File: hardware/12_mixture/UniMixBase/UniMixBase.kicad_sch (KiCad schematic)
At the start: 145 parts, among them IC1 VNN3NV04PTR-E, IC11 VNN3NV04PTR-E, IC2 VNN3NV04PTR-E, IC3 VNN3NV04PTR-E, IC4 VNN3NV04PTR-E, IC5 VNN3NV04PTR-E, IC6 VNN3NV04PTR-E, IC7 VNN3NV04PTR-E, IC8 VNN3NV04PTR-E, J1 Conn_01x04_Male, J10 Conn_01x03_Pin, J11 Conn_01x02_Male, J12 Conn_01x02_Male, J13 Conn_01x02_Male, J14 Conn_01x04_Male, J18 Conn_01x04_Male, J2 Conn_01x04_Male, J20 Conn_01x04_Male, J21 Conn_01x04_Male, J22 Conn_01x03_Pin, J24 Conn_01x04_Male, J3 Conn_01x04_Male, J31 Conn_01x02_Male, J32 Conn_01x02_Male, J33 Conn_01x02_Male, J4 Conn_01x04_Male, J5 Conn_01x04_Male, J6 Conn_01x03_Pin, J7 Conn_01x04_Male, J8 Conn_01x04_Male, J9 Conn_01x04_Male, U1 NUCLEO-H755, U10 74AHC04, U11 MP1584 DC/DC, U12 TCA9802, U13 TMC2209_SILENTSTEPSTICK, U2 TMC2209_SILENTSTEPSTICK, U3 TMC2209_SILENTSTEPSTICK, U4 TMC2209_SILENTSTEPSTICK, U5 74AHC04, U6 TMC2209_SILENTSTEPSTICK, U7 TMC2209_SILENTSTEPSTICK, U8 MP1584 DC/DC, U9 74AHC04

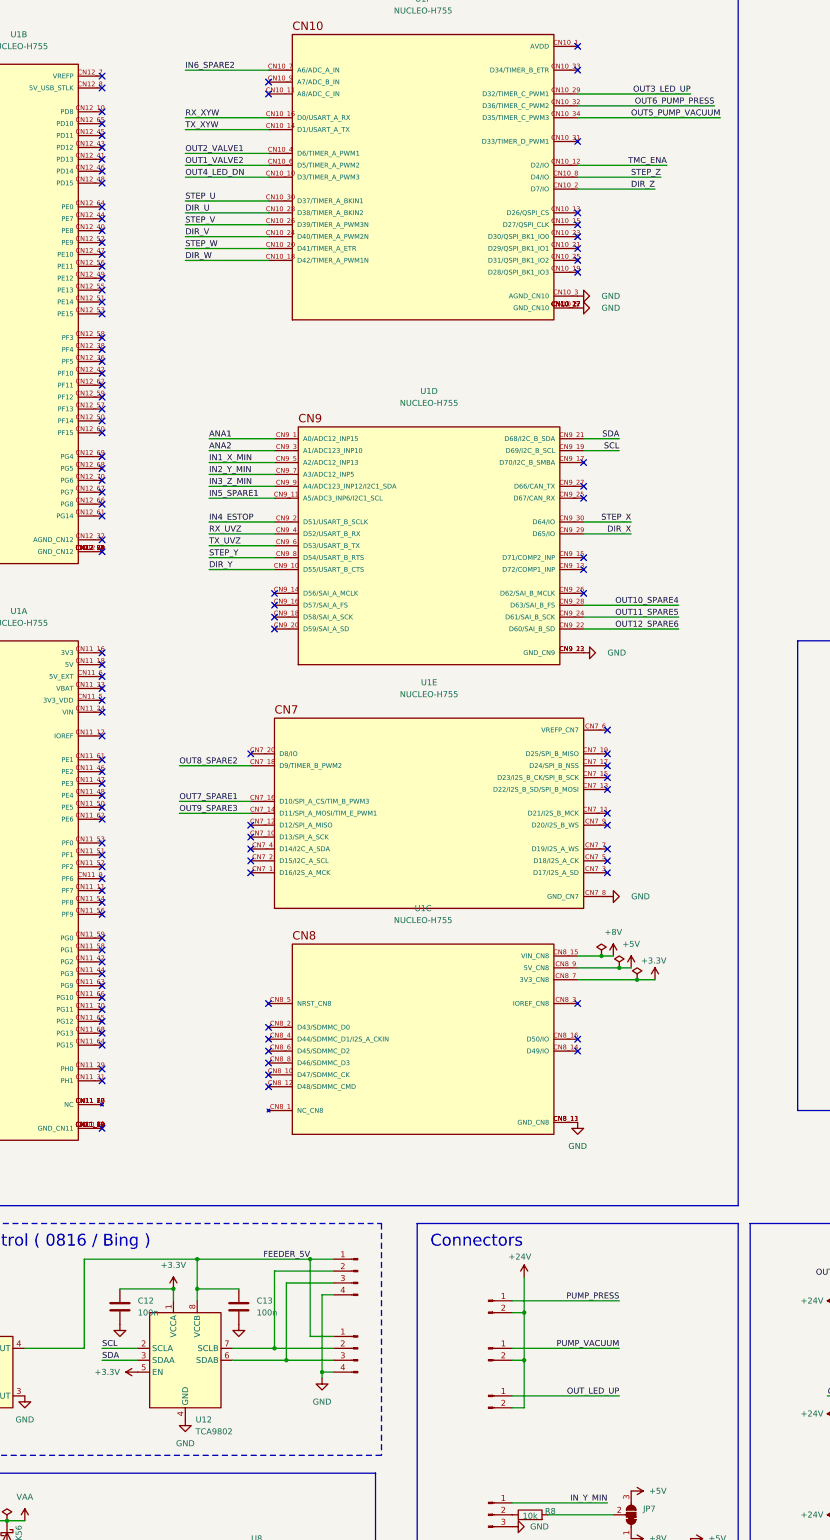
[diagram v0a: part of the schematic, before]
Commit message: Upadtes for Nucleo version
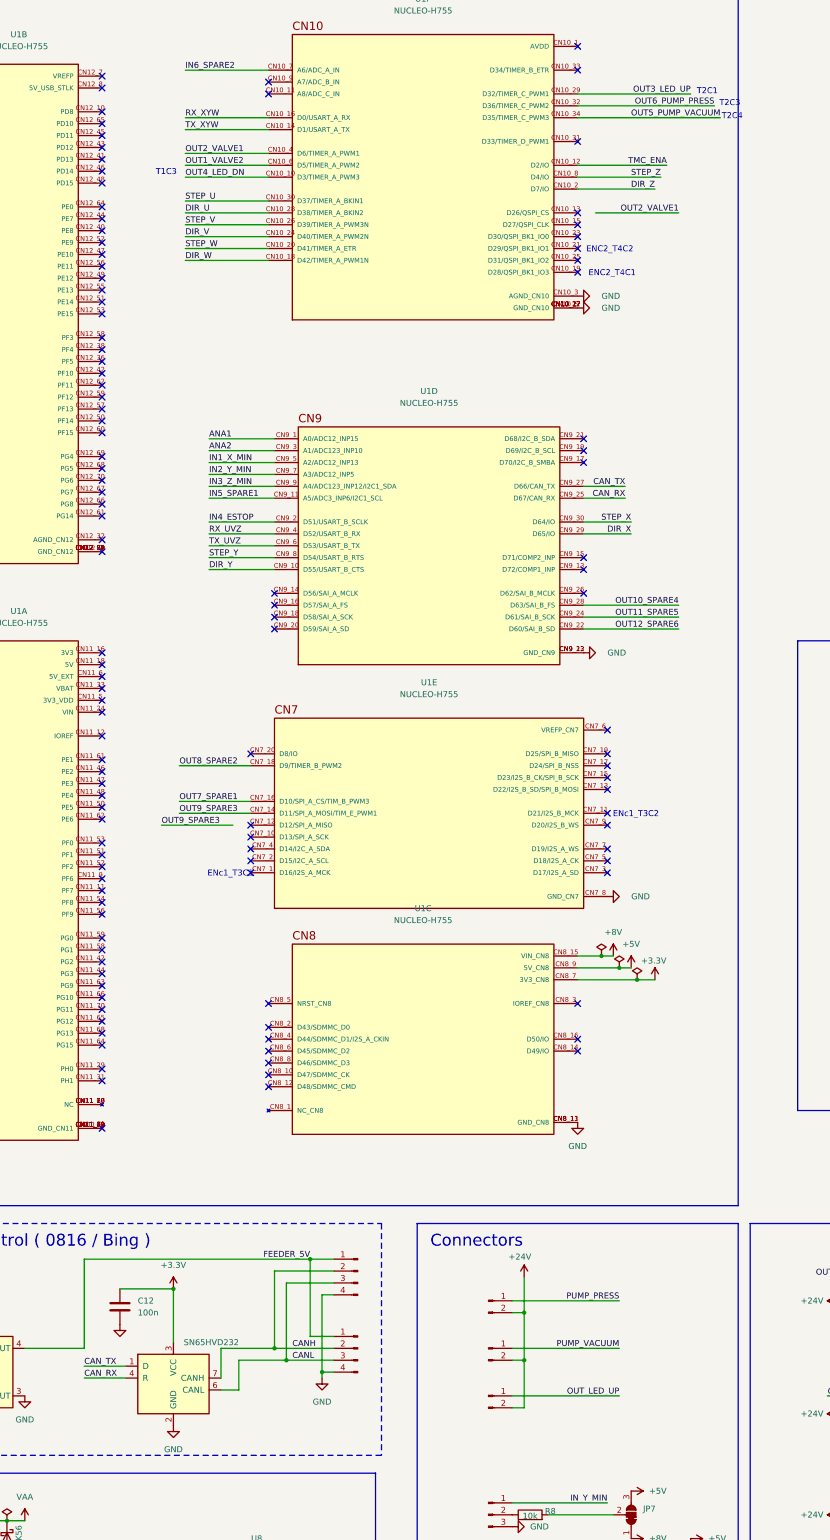
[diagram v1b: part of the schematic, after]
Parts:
- removed C13: 100n, Capacitor_SMD:C_0603_1608Metric, symbol Device:C
- removed U12: TCA9802, Package_SO:VSSOP-8_3x3mm_P0.65mm, symbol Interface:TCA9802
- added U12: SN65HVD232, Package_SO:SOIC-8_3.9x4.9mm_P1.27mm, symbol Interface_CAN_LIN:SN65HVD232
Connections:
- net +3.3V: now also U12.3 (VCC)
- net GND: now also U12.2 (GND)
- net CANL: now reaches J5.3 (Pin_3), J8.3 (Pin_3)
- net CANL: now also U12.6 (CANL)
- net CANH: now reaches J5.2 (Pin_2), J8.2 (Pin_2)
- net CANH: now also U12.7 (CANH)
- net CAN_RX: now reaches U1.CN9_25 (D67/CAN_RX)
- net CAN_RX: now also U12.4 (R)
- net CAN_TX: now reaches U1.CN9_27 (D66/CAN_TX)
- net CAN_TX: now also U12.1 (D)
- net SCL: no longer names the net of U1.CN9_19 (D69/I2C_B_SCL)
- net SDA: no longer names the net of U1.CN9_21 (D68/I2C_B_SDA)
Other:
- note added: "ENC2_T4C1"
- note added: "ENC2_T4C2"
- note added: "ENc1_T3C1"
- note added: "ENc1_T3C2"
- note added: "T1C3"
- note added: "T2C1"
- note added: "T2C3"
- note added: "T2C4"

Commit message: Updated hardware design
Signed-off-by: Jaroslaw Karwik <jaroslaw.karwik@gmail.com>
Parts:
- added C13: 1uF, Capacitor_SMD:C_0603_1608Metric, symbol Device:C
- added C28: 10uF, Capacitor_SMD:C_1206_3216Metric, symbol Device:C
- added C29, C30, C32: 100n, Capacitor_SMD:C_0603_1608Metric, symbol Device:C
- added C31: 100n / 16V, Capacitor_SMD:C_0603_1608Metric, symbol mfc_base_lib:C
- added IC9: AP7375-50W5-7, footprints:SOT95P285X140-5N, symbol AP7375-50W5-7:AP7375-50W5-7
- added J15, J16: Conn_01x06_Male, Connector_JST:JST_XH_B6B-XH-AM_1x06_P2.50mm_Vertical, symbol Connector:Conn_01x06_Pin
- added R48, R49, R50, R51: 120R, Resistor_SMD:R_1206_3216Metric, symbol Device:R
- added U14: AM26LV32xD, Package_SO:SOIC-16_3.9x9.9mm_P1.27mm, symbol Interface:AM26LV32xD
- added U15: TLE9251VSJ, Package_SO:SOIC-8_3.9x4.9mm_P1.27mm, symbol mfc_base_lib:TLE9251VSJ
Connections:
- net +3.3V: now also C29.1, C32.1, U14.16 (VDD), U14.4 (G), U15.5 (VIO)
- net +5V: now also C31.1, U15.3 (VCC)
- net +8V: now also C13.1, IC9.1 (VIN), IC9.3 (EN)
- net CANH: now also U15.7 (CANH)
- net CANL: now also U15.6 (CANL)
- net CAN_RX: now also U15.4 (RXD)
- net CAN_TX: now also U15.1 (TXD)
- net DIR_X: now also U1.CN9_13 (D72/COMP1_INP); no longer U1.CN9_29 (D65/IO)
- net GND: now also C29.2, C31.2, C32.2, J15.6 (Pin_6), J16.6 (Pin_6), U14.12 (~{G}), U14.8 (GND), U15.2 (GND), U15.8 (STB)
- net IN5_SPARE1: now also U1.CN9_14 (D56/SAI_A_MCLK); no longer U1.CN9_11 (A5/ADC3_INP6/I2C1_SCL)
- net IN6_SPARE2: now also U1.CN10_31 (D33/TIMER_D_PWM1); no longer U1.CN10_7 (A6/ADC_A_IN)
- net OUT2_VALVE1: now also U1.CN10_13 (D26/QSPI_CS); no longer U1.CN10_4 (D6/TIMER_A_PWM1)
- net OUT9_SPARE3: now also U1.CN7_12 (D12/SPI_A_MISO); no longer U1.CN7_14 (D11/SPI_A_MOSI/TIM_E_PWM1)
- net STEP_X: now also U1.CN9_15 (D71/COMP2_INP); no longer U1.CN9_30 (D64/IO)
- net ENC2_CH1: now reaches U1.CN10_19 (D28/QSPI_BK1_IO3)
- net ENC2_CH1: now also U14.11 (3Y)
- net ENC2_CH2: now reaches U1.CN10_21 (D29/QSPI_BK1_IO1)
- net ENC2_CH2: now also U14.13 (4Y)
- net ENC1_CH1: now reaches U1.CN7_1 (D16/I2S_A_MCK)
- net ENC1_CH1: now also U14.3 (1Y)
- net ENC1_CH2: now reaches U1.CN7_11 (D21/I2S_B_MCK)
- net ENC1_CH2: now also U14.5 (2Y)
- new net: J15.2 (Pin_2), R48.1, U14.2 (1A)
- new net: J15.3 (Pin_3), R48.2, U14.1 (1B)
- new net: C13.2, C28.2, C30.2, IC9.2 (GND)
- new net: J15.4 (Pin_4), R49.1, U14.6 (2A)
- new net: J15.5 (Pin_5), R49.2, U14.7 (2B)
- new net: J16.2 (Pin_2), R50.1, U14.10 (3A)
- new net: J16.3 (Pin_3), R50.2, U14.9 (3B)
- new net: J16.4 (Pin_4), R51.1, U14.14 (4A)
- new net: J16.5 (Pin_5), R51.2, U14.15 (4B)
- new net +5VA: C28.1, C30.1, IC9.5 (VOUT), J15.1 (Pin_1), J16.1 (Pin_1)
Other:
- note added: "(T1C3)"
- note added: "(T2C1)"
- note added: "(T2C3)"
- note added: "(T2C4)"
- note added: "(T3C1)"
- note added: "(T3C2)"
- note added: "(T4C1)"
- note added: "(T4C2)"
- note added: "Optional FDCAN"
- note added: "X/Y encoders (optional)"
- note removed: "ENC2_T4C1"
- note removed: "ENC2_T4C2"
- note removed: "ENc1_T3C1"
- note removed: "ENc1_T3C2"
- note removed: "T1C3"
- note removed: "T2C1"
- note removed: "T2C3"
- note removed: "T2C4"
- moved on the sheet: C10, C11, C12, C26, C7, C9, D1, D3A, D3B, D5, D6, D7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

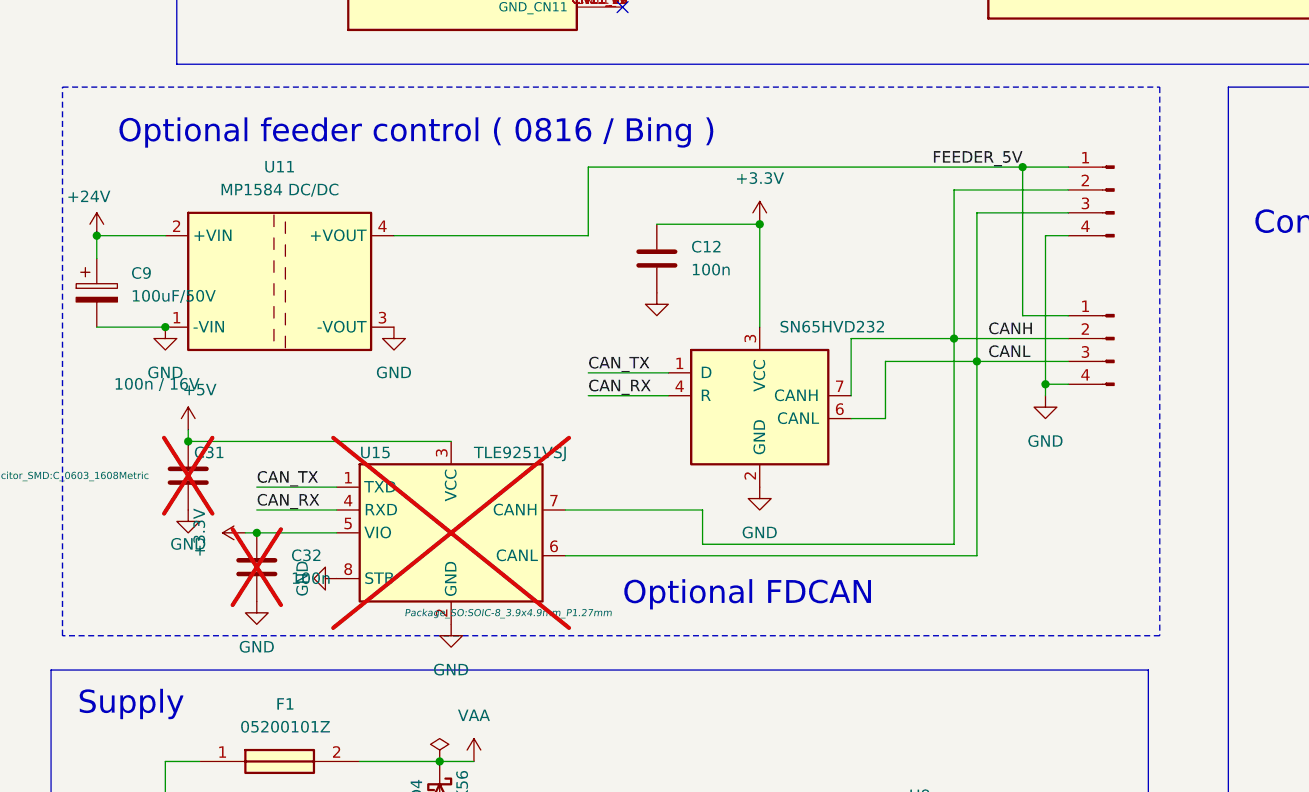
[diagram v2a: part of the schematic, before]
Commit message: CAN FD head added
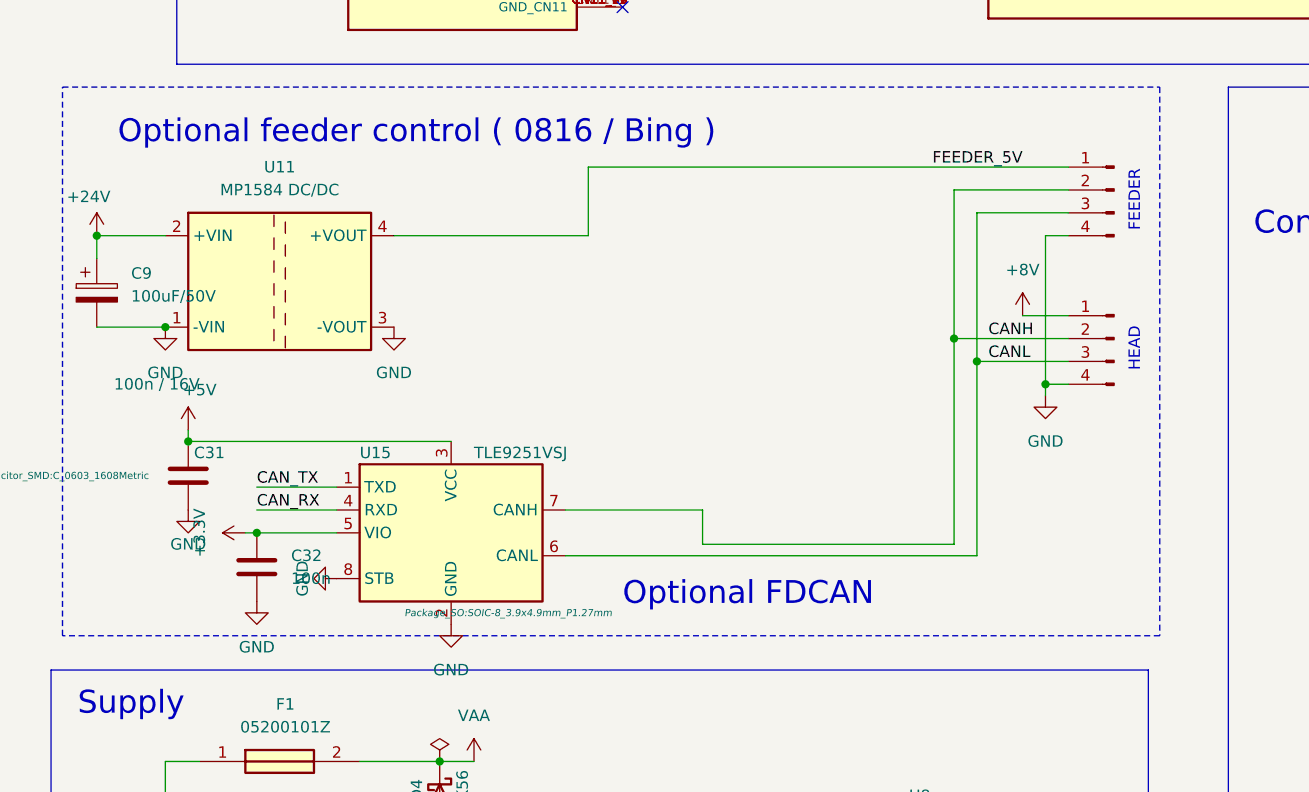
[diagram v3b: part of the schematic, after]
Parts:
- removed C12: 100n, Capacitor_SMD:C_0603_1608Metric, symbol Device:C
- removed U12: SN65HVD232, Package_SO:SOIC-8_3.9x4.9mm_P1.27mm, symbol Interface_CAN_LIN:SN65HVD232
- C31, C32, U15: now fitted
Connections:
- net +8V: now also J8.1 (Pin_1)
- net FEEDER_5V: no longer J8.1 (Pin_1)
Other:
- note added: "FEEDER"
- note added: "HEAD"
